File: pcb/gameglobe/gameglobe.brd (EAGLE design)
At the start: 98.4 x 49.5 mm, 16 parts

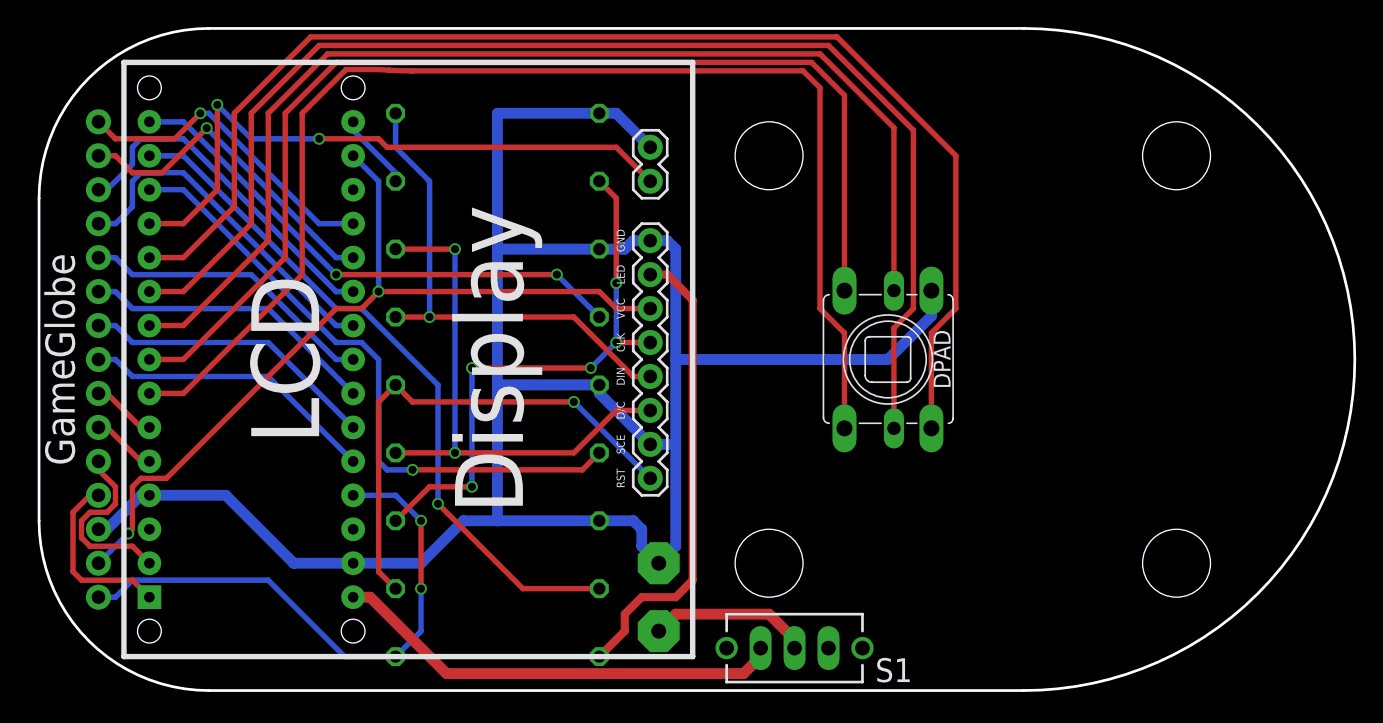
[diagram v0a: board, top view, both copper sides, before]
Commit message: Add QR code; Reduce top corner radiuses; Fix/improve some routing things;
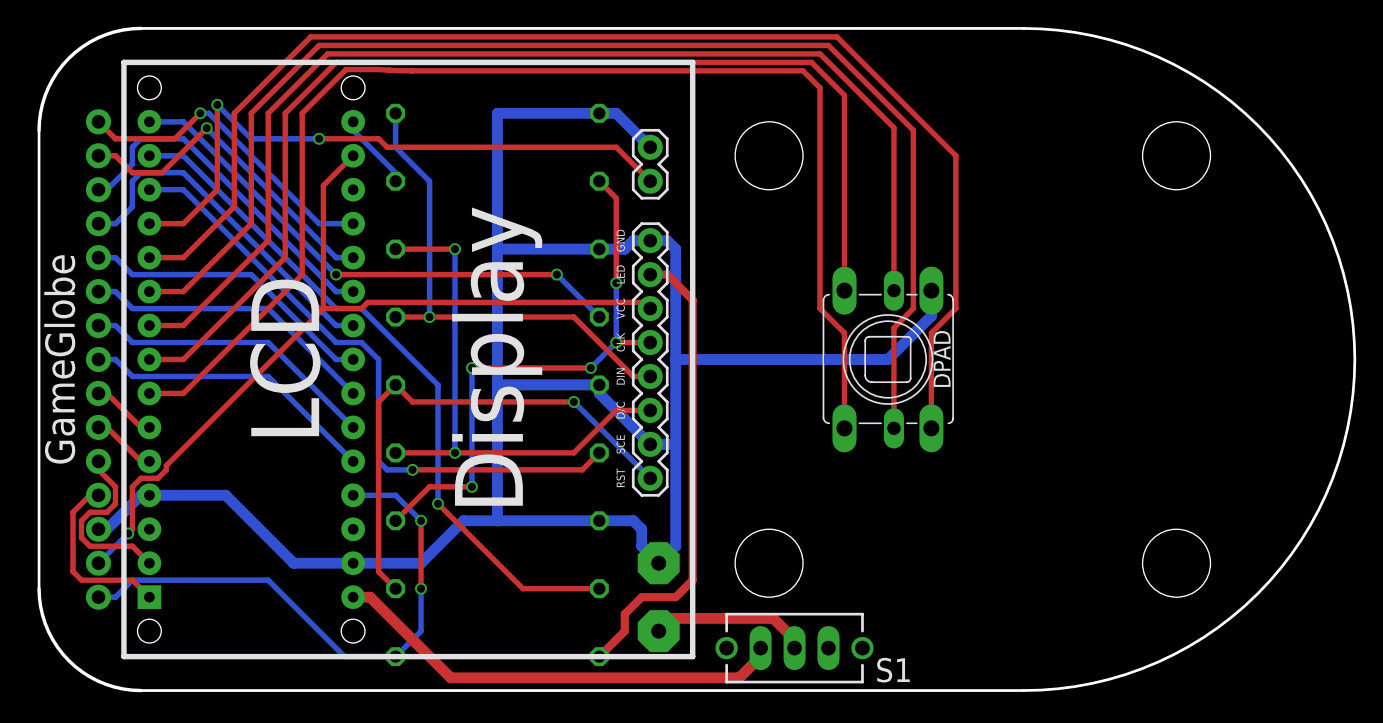
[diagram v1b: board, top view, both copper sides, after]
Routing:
- net 3V3: track 63.0 -> 63.9 mm, vias 2 -> 1
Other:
- outline, holes or cut-outs redrawn
- board text added: "http://v.ht/3310"

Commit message: change wiring to use different pins for the speaker with ToneAC library (and also all the buttons)
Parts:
- JP2: device SparkFun-Connectors:1X15 -> SparkFun-Connectors:1X14-LONGPADS
- moved JP3 2.54 mm to (45.7, 38.7), turned to 90 degrees
- moved JP2 1.27 mm to (4.45, 8.89)
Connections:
- removed net N$19: ARDUINO_NANO.D3, JP2.7
- removed net SPKR: ARDUINO_NANO.D9, JP3.2
- new net N$10: ARDUINO_NANO.D10, JP3.2
- new net N$20: ARDUINO_NANO.D8, R12.1
- net DPAD_CENTER: now also ARDUINO_NANO.D3; no longer ARDUINO_NANO.D5
- net DPAD_DOWN: now also ARDUINO_NANO.D6; no longer ARDUINO_NANO.D8
- net DPAD_LEFT: now also ARDUINO_NANO.D5; no longer ARDUINO_NANO.D7
- net DPAD_RIGHT: now also ARDUINO_NANO.D4; no longer ARDUINO_NANO.D6
- net DPAD_UP: now also ARDUINO_NANO.D2; no longer ARDUINO_NANO.D4
- net GND: no longer JP3.1
- net N$11: now also JP2.7; no longer JP2.8
- net N$12: now also JP2.8; no longer JP2.9
- net N$13: now also JP2.9; no longer JP2.10
- net N$14: now also JP2.10; no longer JP2.11
- net N$15: now also JP2.11; no longer JP2.12
- net N$16: now also JP2.12; no longer JP2.13
- net N$17: now also JP2.13; no longer JP2.14
- net N$18: now also JP2.14; no longer JP2.15
- net N$4: now also ARDUINO_NANO.D9, JP3.1; no longer ARDUINO_NANO.D10, R12.1
- net N$9: now also ARDUINO_NANO.D7; no longer ARDUINO_NANO.D2
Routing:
- net N$10: track 0.00 -> 48.1 mm, vias 0 -> 1
- net SPKR: track 47.2 -> 0.00 mm, vias 2 -> 0
- net N$20: track 0.00 -> 43.7 mm, vias 0 -> 1
- net N$9: track 4.86 -> 15.8 mm
- net GND: track 167.2 -> 161.8 mm
- net DPAD_CENTER: track 83.2 -> 88.2 mm
- net DPAD_RIGHT: track 84.2 -> 89.2 mm
- net DPAD_LEFT: track 95.1 -> 100.2 mm
- net DPAD_DOWN: track 96.1 -> 101.2 mm
- net DPAD_UP: track 94.0 -> 99.1 mm
- net N$19: track 4.86 -> 0.00 mm
- net N$3: track 52.3 -> 57.1 mm, vias 1 -> 5
- net N$15: track 26.5 -> 21.7 mm
- net N$16: track 26.1 -> 21.7 mm
- net N$7: track 13.4 -> 17.0 mm
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
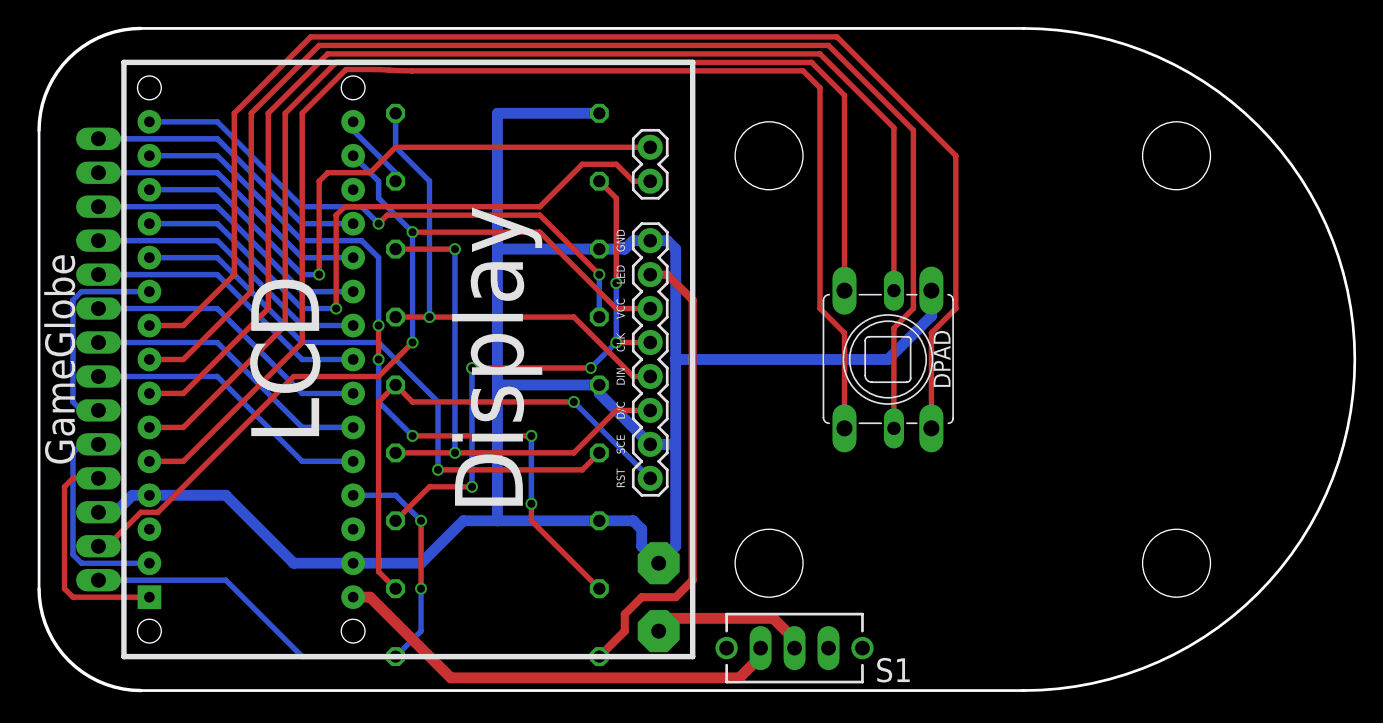
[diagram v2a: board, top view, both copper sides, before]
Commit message: change pin numbers (just as in the code, see previous commit), also use ground plane
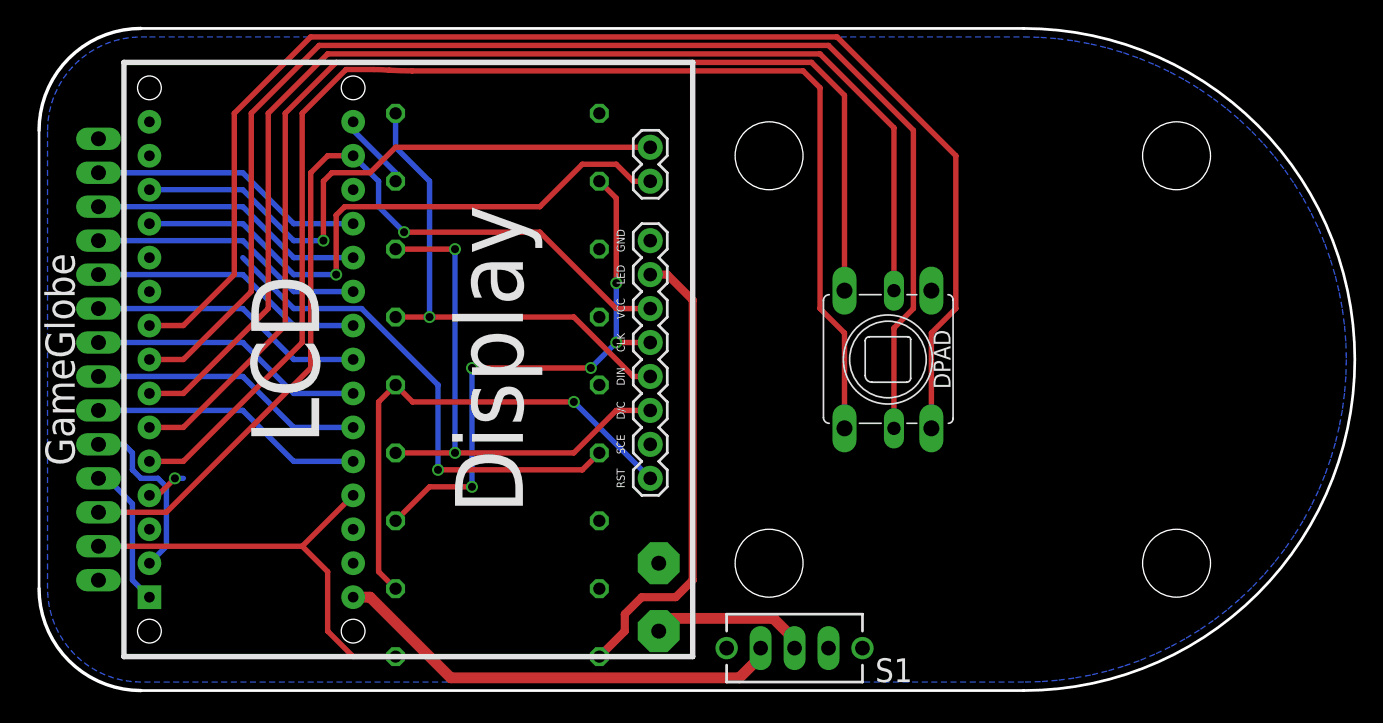
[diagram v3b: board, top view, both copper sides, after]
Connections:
- removed net N$9: ARDUINO_NANO.D7, JP2.6
- net 3V3: now also JP2.3; no longer JP2.2
- net 5V: now also JP2.2; no longer JP2.1
- net GND: now also JP2.1, JP2.14; no longer JP2.3
- net N$11: now also JP2.6; no longer JP2.7
- net N$12: now also JP2.7; no longer JP2.8
- net N$13: now also JP2.8; no longer JP2.9
- net N$14: now also JP2.9; no longer JP2.10
- net N$15: now also JP2.10; no longer JP2.11
- net N$16: now also JP2.11; no longer JP2.12
- net N$17: now also JP2.12; no longer JP2.13
- net N$18: now also JP2.13; no longer JP2.14
- net N$2: now also ARDUINO_NANO.D11; no longer ARDUINO_NANO.D12
- net N$20: now also ARDUINO_NANO.D7; no longer ARDUINO_NANO.D8
- net N$3: now also ARDUINO_NANO.D8; no longer ARDUINO_NANO.D11
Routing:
- net GND: track 161.8 -> 3.07 mm, vias 0 -> 1
- net N$3: track 57.1 -> 0.00 mm, vias 5 -> 0
- net N$2: track 42.1 -> 0.00 mm, vias 2 -> 0
- net N$9: track 15.8 -> 0.00 mm
- net 5V: track 41.4 -> 33.6 mm, vias 2 -> 0
- net N$20: track 43.7 -> 37.5 mm
- net N$7: track 17.0 -> 10.8 mm
- net N$10: track 48.1 -> 44.5 mm
- net N$4: track 49.2 -> 45.6 mm
- net N$8: track 15.8 -> 13.4 mm
- net N$16: track 21.7 -> 20.6 mm
- net N$15: track 21.7 -> 20.6 mm
- net N$12: track 21.7 -> 20.6 mm
- net N$11: track 21.7 -> 20.6 mm
- net N$18: track 21.7 -> 20.6 mm
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- added copper zone on layer 16, net GND

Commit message: Add power planes for 3V3 and 5V to add a more premium feeling to the board design (whatever this may mean)
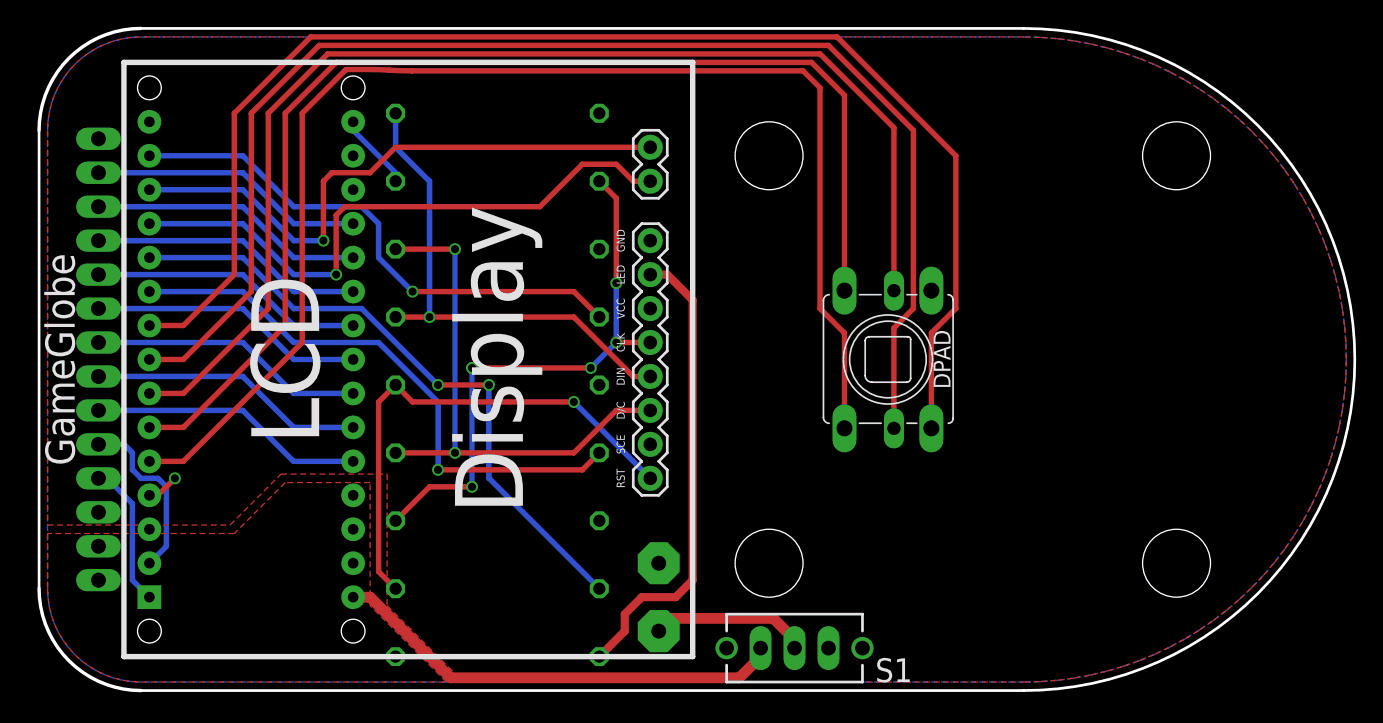
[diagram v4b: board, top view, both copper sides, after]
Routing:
- net 3V3: track 66.7 -> 0.00 mm, vias 1 -> 0
- net N$3: track 0.00 -> 48.0 mm, vias 0 -> 2
- net N$2: track 0.00 -> 40.1 mm, vias 0 -> 1
- net 5V: track 33.6 -> 0.00 mm
- net N$20: track 37.5 -> 42.7 mm
- net GND: track 3.07 -> 2.43 mm
- added copper zone on layer 1, net 3V3
- added copper zone on layer 1, net 5V
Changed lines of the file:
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@@
 <setting verticaltext="up"/>
 </settings>
-<grid distance="25" unitdist="mil" unit="mil" style="lines" multiple="1" display="yes" altdistance="6.25" altunitdist="mil" altunit="mil"/>
+<grid distance="12.5" unitdist="mil" unit="mil" style="lines" multiple="1" display="yes" altdistance="6.25" altunitdist="mil" altunit="mil"/>
 <layers>
 <layer number="1" name="Top" color="4" fill="1" visible="yes" active="yes"/>
@@
 </elements>
 <signals>
-<signal name="GND">
-<contactref element="JP1" pad="8"/>
-<contactref element="JP1" pad="2"/>
-<contactref element="R14" pad="1"/>
-<contactref element="R15" pad="1"/>
-<contactref element="R16" pad="1"/>
-<contactref element="DPAD" pad="COMMON"/>
-<contactref element="ARDUINO_NANO" pad="GND1"/>
-<contactref element="ARDUINO_NANO" pad="GND"/>
-<contactref element="R13" pad="1"/>
-<contactref element="BATTERY" pad="-"/>
-<contactref element="JP2" pad="1"/>
-<contactref element="JP2" pad="14"/>
-<polygon width="0.4064" layer="16" isolate="0.3048">
-<vertex x="24.13" y="1.27"/>
-<vertex x="7.62" y="1.27" curve="-90"/>
-<vertex x="0.635" y="8.255"/>
-<vertex x="0.635" y="42.545" curve="-90"/>
-<vertex x="7.62" y="49.53"/>
-<vertex x="8.255" y="49.53"/>
-<vertex x="73.66" y="49.53" curve="-90"/>
-<vertex x="97.79" y="25.4" curve="-90"/>
-<vertex x="73.66" y="1.27"/>
-</polygon>
-<wire x1="8.255" y1="15.24" x2="8.89" y2="15.24" width="0.4064" layer="1"/>
-<wire x1="8.89" y1="15.24" x2="10.16" y2="16.51" width="0.4064" layer="1"/>
-<via x="10.16" y="16.51" extent="1-16" drill="0.6"/>
-<wire x1="10.16" y1="16.51" x2="10.795" y2="16.51" width="0.4064" layer="16"/>
-</signal>
 <signal name="LCD_RST">
 <contactref element="JP1" pad="1"/>
@@
 <contactref element="JP1" pad="6"/>
 <contactref element="ARDUINO_NANO" pad="3V3"/>
-<wire x1="23.495" y1="40.64" x2="25.4" y2="38.735" width="0.4064" layer="16"/>
-<wire x1="25.4" y1="38.735" x2="25.4" y2="36.83" width="0.4064" layer="16"/>
-<wire x1="25.4" y1="36.83" x2="27.305" y2="34.925" width="0.4064" layer="16"/>
-<via x="27.305" y="34.925" extent="1-16" drill="0.6"/>
-<wire x1="27.305" y1="34.925" x2="37.465" y2="34.925" width="0.4064" layer="1"/>
-<wire x1="37.465" y1="34.925" x2="43.18" y2="29.21" width="0.4064" layer="1"/>
-<wire x1="43.18" y1="29.21" x2="45.72" y2="29.21" width="0.4064" layer="1"/>
 <contactref element="JP2" pad="3"/>
-<wire x1="20.32" y1="24.765" x2="9.525" y2="13.97" width="0.4064" layer="1"/>
-<wire x1="9.525" y1="13.97" x2="4.445" y2="13.97" width="0.4064" layer="1"/>
-<wire x1="20.32" y1="24.765" x2="20.32" y2="39.37" width="0.4064" layer="1"/>
-<wire x1="20.32" y1="39.37" x2="21.59" y2="40.64" width="0.4064" layer="1"/>
-<wire x1="21.59" y1="40.64" x2="23.495" y2="40.64" width="0.4064" layer="1"/>
+<polygon width="0.254" layer="1" isolate="0.254">
+<vertex x="0.635" y="13.0175"/>
+<vertex x="14.2875" y="13.0175"/>
+<vertex x="18.0975" y="16.8275"/>
+<vertex x="26.035" y="16.8275"/>
+<vertex x="26.035" y="6.985"/>
+<vertex x="31.75" y="1.27"/>
+<vertex x="73.66" y="1.27" curve="90"/>
+<vertex x="97.79" y="25.4" curve="90"/>
+<vertex x="73.66" y="49.53"/>
+<vertex x="7.62" y="49.53" curve="90"/>
+<vertex x="0.635" y="42.545"/>
+</polygon>
 </signal>
 <signal name="LCD_LED">
@@
 <contactref element="ARDUINO_NANO" pad="+5V"/>
 <contactref element="JP2" pad="2"/>
-<wire x1="4.445" y1="11.43" x2="19.685" y2="11.43" width="0.4064" layer="1"/>
-<wire x1="19.685" y1="11.43" x2="23.495" y2="15.24" width="0.4064" layer="1"/>
-<wire x1="26.67" y1="3.175" x2="23.495" y2="3.175" width="0.4064" layer="1"/>
-<wire x1="23.495" y1="3.175" x2="21.59" y2="5.08" width="0.4064" layer="1"/>
-<wire x1="21.59" y1="5.08" x2="21.59" y2="9.525" width="0.4064" layer="1"/>
-<wire x1="21.59" y1="9.525" x2="19.685" y2="11.43" width="0.4064" layer="1"/>
+<polygon width="0.254" layer="1" isolate="0.254">
+<vertex x="0.635" y="12.3825"/>
+<vertex x="0.635" y="8.255" curve="90"/>
+<vertex x="7.62" y="1.27"/>
+<vertex x="30.48" y="1.27"/>
+<vertex x="24.765" y="6.985"/>
+<vertex x="24.765" y="16.1925"/>
+<vertex x="18.415" y="16.1925"/>
+<vertex x="14.605" y="12.3825"/>
+</polygon>
 </signal>
 <signal name="DPAD_DOWN">
@@
 <contactref element="R12" pad="1"/>
 <via x="29.845" y="17.145" extent="1-16" drill="0.6"/>
-<wire x1="29.845" y1="23.495" x2="29.845" y2="17.145" width="0.4064" layer="16"/>
+<wire x1="29.845" y1="22.225" x2="29.845" y2="17.145" width="0.4064" layer="16"/>
 <wire x1="29.845" y1="17.145" x2="40.64" y2="17.145" width="0.4064" layer="1"/>
 <wire x1="40.64" y1="17.145" x2="41.91" y2="18.415" width="0.4064" layer="1"/>
-<wire x1="24.13" y1="29.21" x2="29.845" y2="23.495" width="0.4064" layer="16"/>
-<wire x1="24.13" y1="29.21" x2="19.05" y2="29.21" width="0.4064" layer="16"/>
-<wire x1="19.05" y1="29.21" x2="15.24" y2="33.02" width="0.4064" layer="16"/>
+<wire x1="25.4" y1="26.67" x2="29.845" y2="22.225" width="0.4064" layer="16"/>
+<wire x1="25.4" y1="26.67" x2="19.05" y2="26.67" width="0.4064" layer="16"/>
+<wire x1="19.05" y1="26.67" x2="15.24" y2="30.48" width="0.4064" layer="16"/>
 <contactref element="ARDUINO_NANO" pad="D7"/>
-<wire x1="8.255" y1="30.48" x2="15.24" y2="33.02" width="0" layer="19" extent="16-16"/>
+<wire x1="15.24" y1="30.48" x2="8.255" y2="30.48" width="0.4064" layer="16"/>
 </signal>
 <signal name="N$2">
 <contactref element="ARDUINO_NANO" pad="D11"/>
 <contactref element="R10" pad="1"/>
-<wire x1="8.255" y1="40.64" x2="41.91" y2="28.575" width="0" layer="19" extent="1-1"/>
+<wire x1="8.255" y1="40.64" x2="15.24" y2="40.64" width="0.4064" layer="16"/>
+<wire x1="15.24" y1="40.64" x2="19.05" y2="36.83" width="0.4064" layer="16"/>
+<wire x1="19.05" y1="36.83" x2="24.13" y2="36.83" width="0.4064" layer="16"/>
+<wire x1="24.13" y1="36.83" x2="25.4" y2="35.56" width="0.4064" layer="16"/>
+<wire x1="25.4" y1="35.56" x2="25.4" y2="33.02" width="0.4064" layer="16"/>
+<wire x1="25.4" y1="33.02" x2="27.94" y2="30.48" width="0.4064" layer="16"/>
+<via x="27.94" y="30.48" extent="1-16" drill="0.6"/>
+<wire x1="27.94" y1="30.48" x2="40.005" y2="30.48" width="0.4064" layer="1"/>
+<wire x1="40.005" y1="30.48" x2="41.91" y2="28.575" width="0.4064" layer="1"/>
 </signal>
 <signal name="N$3">
 <contactref element="R11" pad="1"/>
 <contactref element="ARDUINO_NANO" pad="D8"/>
-<wire x1="8.255" y1="33.02" x2="41.91" y2="8.255" width="0" layer="19" extent="1-1"/>
+<wire x1="8.255" y1="33.02" x2="15.24" y2="33.02" width="0.4064" layer="16"/>
+<wire x1="15.24" y1="33.02" x2="19.05" y2="29.21" width="0.4064" layer="16"/>
+<wire x1="19.05" y1="29.21" x2="24.13" y2="29.21" width="0.4064" layer="16"/>
+<wire x1="24.13" y1="29.21" x2="29.845" y2="23.495" width="0.4064" layer="16"/>
+<via x="29.845" y="23.495" extent="1-16" drill="0.6"/>
+<wire x1="29.845" y1="23.495" x2="33.655" y2="23.495" width="0.4064" layer="1"/>
+<via x="33.655" y="23.495" extent="1-16" drill="0.6"/>
+<wire x1="33.655" y1="23.495" x2="33.655" y2="16.51" width="0.4064" layer="16"/>
+<wire x1="33.655" y1="16.51" x2="41.91" y2="8.255" width="0.4064" layer="16"/>
+</signal>
+<signal name="GND">
+<polygon width="0.254" layer="16" isolate="0.254">
+<vertex x="24.13" y="1.27"/>
+<vertex x="7.62" y="1.27" curve="-90"/>
+<vertex x="0.635" y="8.255"/>
+<vertex x="0.635" y="42.545" curve="-90"/>
+<vertex x="7.62" y="49.53"/>
+<vertex x="8.255" y="49.53"/>
+<vertex x="73.66" y="49.53" curve="-90"/>
+<vertex x="97.79" y="25.4" curve="-90"/>
+<vertex x="73.66" y="1.27"/>
+</polygon>
+<contactref element="ARDUINO_NANO" pad="GND1"/>
+<contactref element="R13" pad="1"/>
+<contactref element="BATTERY" pad="-"/>
+<contactref element="JP2" pad="1"/>
+<contactref element="JP2" pad="14"/>
+<contactref element="JP1" pad="8"/>
+<contactref element="JP1" pad="2"/>
+<contactref element="R14" pad="1"/>
+<contactref element="R15" pad="1"/>
+<contactref element="R16" pad="1"/>
+<contactref element="DPAD" pad="COMMON"/>
+<contactref element="ARDUINO_NANO" pad="GND"/>
+<wire x1="8.255" y1="15.24" x2="8.89" y2="15.24" width="0.4064" layer="1"/>
+<wire x1="8.89" y1="15.24" x2="10.16" y2="16.51" width="0.4064" layer="1"/>
+<via x="10.16" y="16.51" extent="1-16" drill="0.6"/>
 </signal>
 </signals>
